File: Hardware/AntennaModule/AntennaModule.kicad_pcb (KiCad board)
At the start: 2 copper layers, 70 x 70 mm, 18 parts

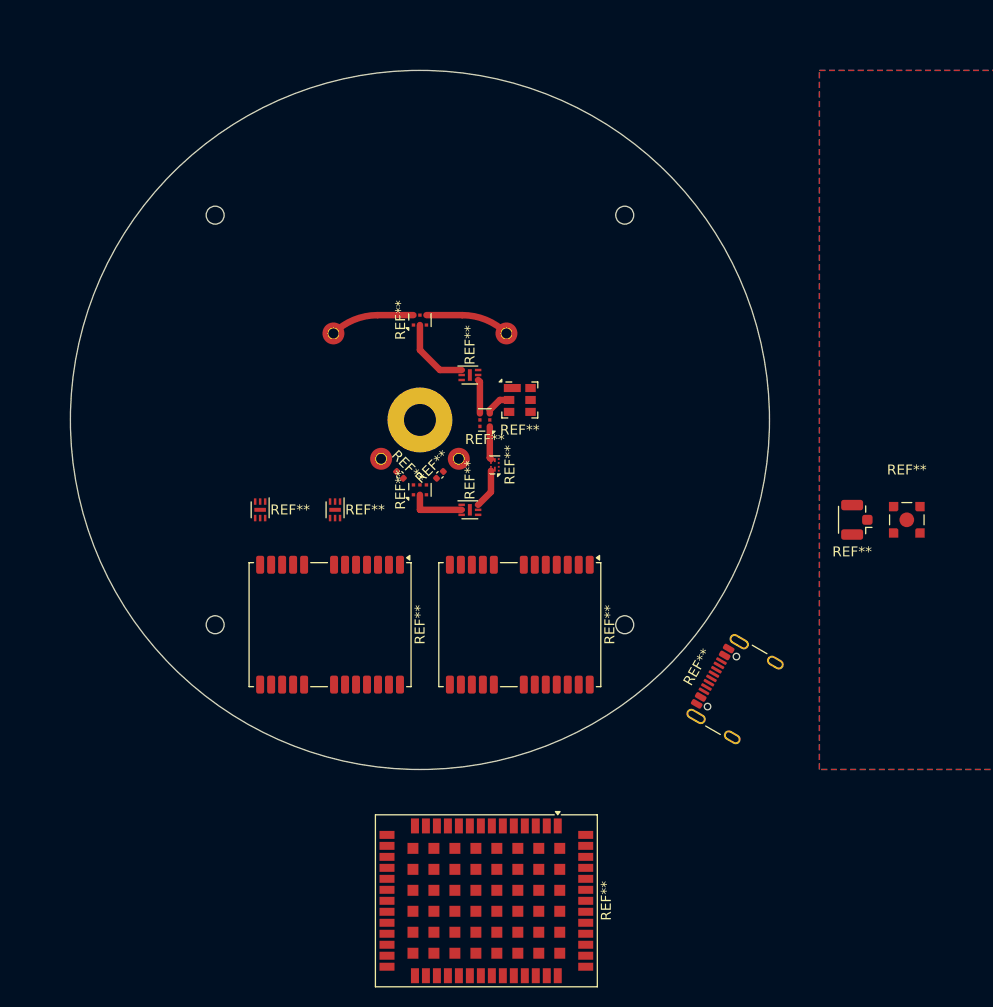
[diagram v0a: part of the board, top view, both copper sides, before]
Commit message: TE0149AをTE0133Bに変更
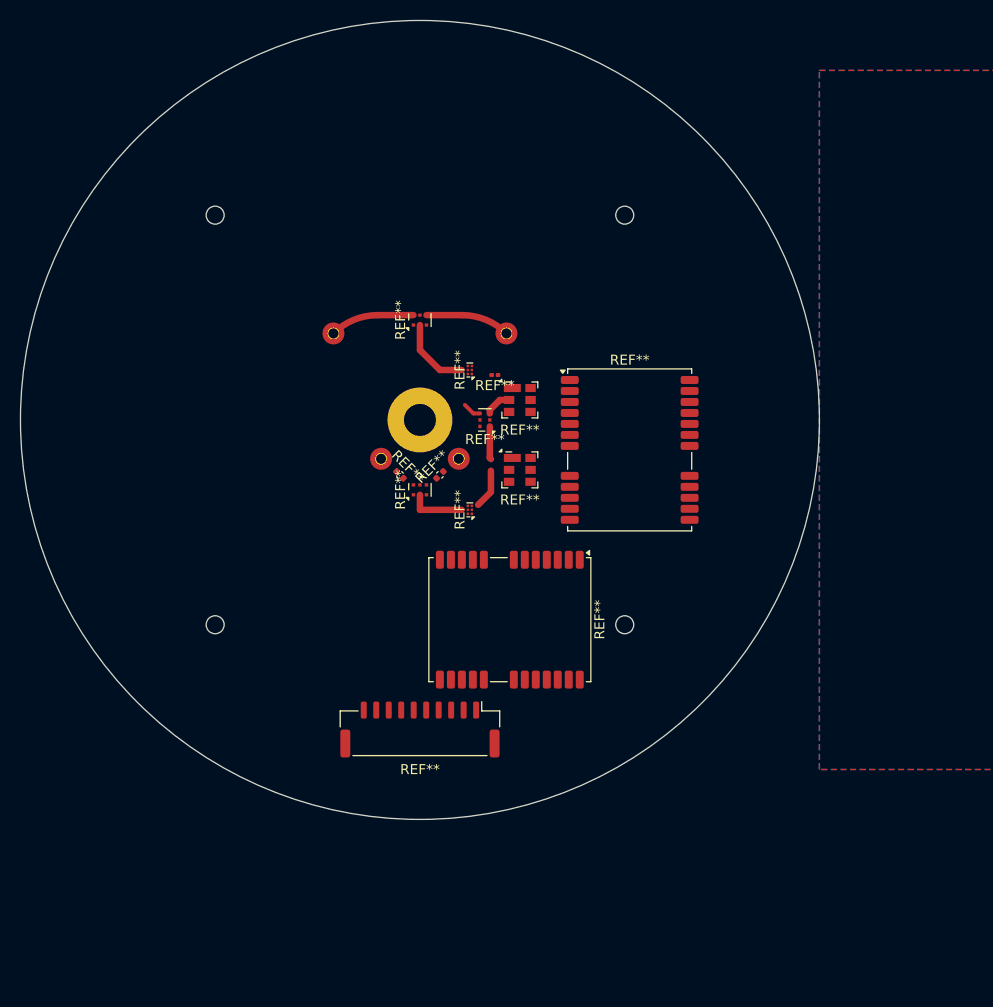
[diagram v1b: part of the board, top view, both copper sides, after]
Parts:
- removed the REF** at (150.0, 95.5)
- removed the REF** at (151.7, 148.2)
- removed the REF** at (193.8, 110.0)
- removed the REF** at (150.0, 109.0)
- removed the REF** at (152.5, 104.5)
- removed the REF** at (177.5, 127.5)
- removed the REF** at (188.8, 110.0)
- removed the REF** at (129.0, 109.0)
- removed the REF** at (136.5, 109.0)
- added REF**: JST_GH_BM10B-GHS-TBT_1x10-1MP_P1.25mm_Vertical, Connector_JST:JST_GH_BM10B-GHS-TBT_1x10-1MP_P1.25mm_Vertical, F.Cu at (145.0, 131.0)
- added REF**: Filter_SAW-6_3.0x3.0mm, Filter_extlib:Filter_SAW-6_3.0x3.0mm, F.Cu at (155.0, 105.0)
- added REF**: Nisshinbo_EPFFP-6-FA, RF_LNA_extlib:Nisshinbo_EPFFP-6-FA, F.Cu at (150.0, 95.0)
- added REF**: C_0201_0603Metric, Capacitor_SMD:C_0201_0603Metric, F.Cu at (152.5, 95.5)
- added REF**: Nisshinbo_EPFFP-6-FA, RF_LNA_extlib:Nisshinbo_EPFFP-6-FA, F.Cu at (150.0, 109.0)
- moved REF** 34.7 mm to (166.0, 103.0), turned to 0 degrees
- moved REF** 1.12 mm to (154.0, 120.0)
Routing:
- net (no net): track 43.5 -> 41.9 mm
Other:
- board size 70 x 70 mm -> 80 x 80 mm
- copper layers 2 -> 4

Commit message: 回路図完成
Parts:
- removed the REF** at (145.0, 131.0)
- removed the REF** at (151.5, 100.0)
- removed the REF** at (145.0, 107.0)
- removed the REF** at (166.0, 103.0)
- removed the REF** at (155.0, 105.0)
- removed the REF** at (145.0, 100.0)
- removed the REF** at (150.0, 95.0)
- removed the REF** at (152.5, 95.5)
- removed the REF** at (143.0, 105.5)
- removed the REF** at (150.0, 109.0)
- removed the REF** at (147.0, 105.5)
- removed the REF** at (155.0, 98.0)
- removed the REF** at (145.0, 90.0)
- removed the REF** at (154.0, 120.0)
- added REF**: L_Murata_LQW15ANxxxx80x_0402_1005Metric_1.0x0.6mm, Inductor_SMD_extlib:L_Murata_LQW15ANxxxx80x_0402_1005Metric_1.0x0.6mm, F.Cu at (150.6, 92.5)
- added REF**: Nisshinbo_EPFFP-6-FA, RF_LNA_extlib:Nisshinbo_EPFFP-6-FA, F.Cu at (152.0, 92.5)
- added REF**: Filter_SAW-6_3.0x3.0mm, Filter_extlib:Filter_SAW-6_3.0x3.0mm, F.Cu at (140.0, 100.0)
- added REF**: C_0402_1005Metric, Capacitor_SMD:C_0402_1005Metric, F.Cu at (153.2, 92.5)
- added REF**: Xinger_0805_2012Metric-6_Pad0.33x0.35mm, RF_Converter_extlib:Xinger_0805_2012Metric-6_Pad0.33x0.35mm, F.Cu at (143.0, 92.5)
- added REF**: Xinger_0805_2012Metric-6_Pad0.33x0.41mm, RF_Converter_extlib:Xinger_0805_2012Metric-6_Pad0.33x0.41mm, F.Cu at (156.5, 95.5)
- added REF**: R_Vishay_FC0603xxxxxxTxx_0603_1608Metric_1.626x0.813mm, Resistor_SMD_extlib:R_Vishay_FC0603xxxxxxTxx_0603_1608Metric_1.626x0.813mm, F.Cu at (158.0, 95.5)
- added REF**: L_Murata_LQW15ANxxxx80x_0402_1005Metric_1.0x0.6mm, Inductor_SMD_extlib:L_Murata_LQW15ANxxxx80x_0402_1005Metric_1.0x0.6mm, F.Cu at (145.0, 100.0)
- added REF**: C_0603_1608Metric, Capacitor_SMD:C_0603_1608Metric, F.Cu at (154.8, 92.5)
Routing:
- net (no net): track 41.9 -> 19.2 mm
- removed copper zone on B.Cu, net (none)
- removed copper zone on F.Cu, net (none)
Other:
- board outline removed
- copper layers 4 -> 2
- board text removed: "coupled"

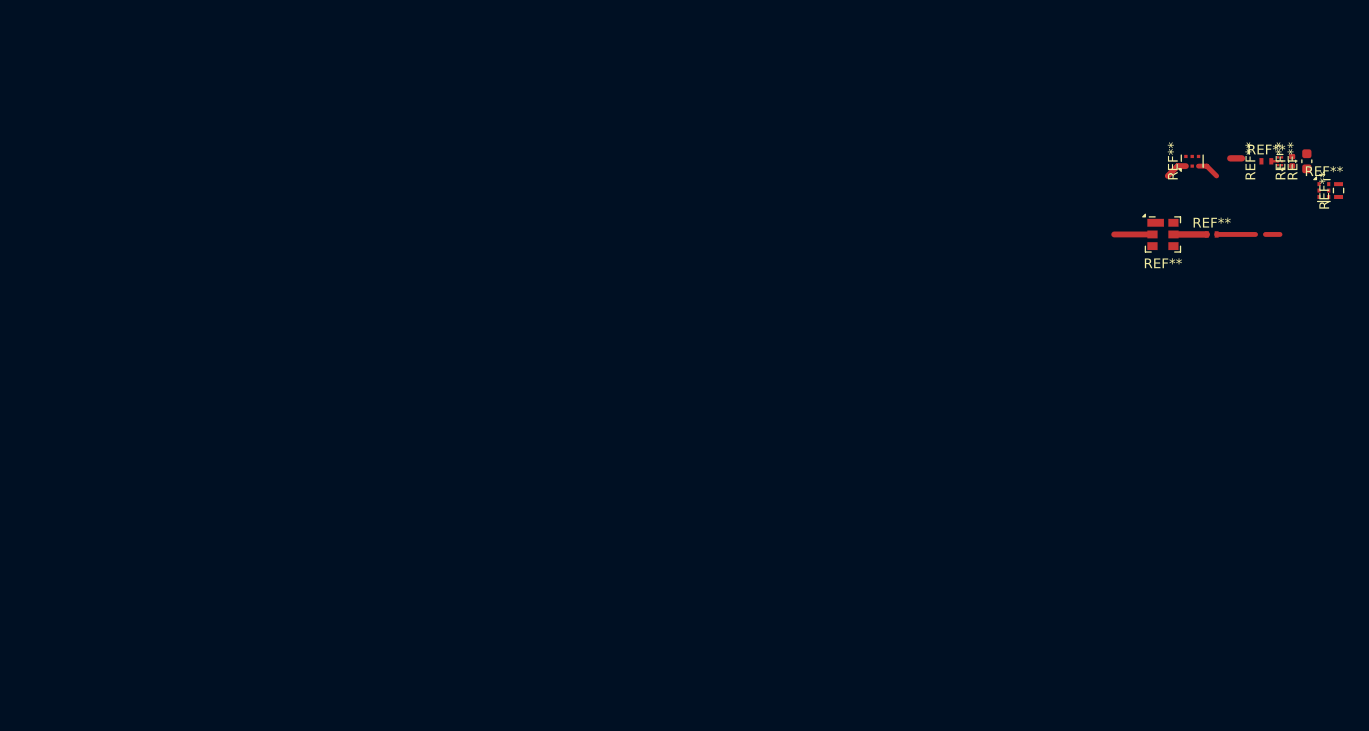
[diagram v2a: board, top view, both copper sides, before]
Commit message: アンテナの給電点が逆になっていたのを修正
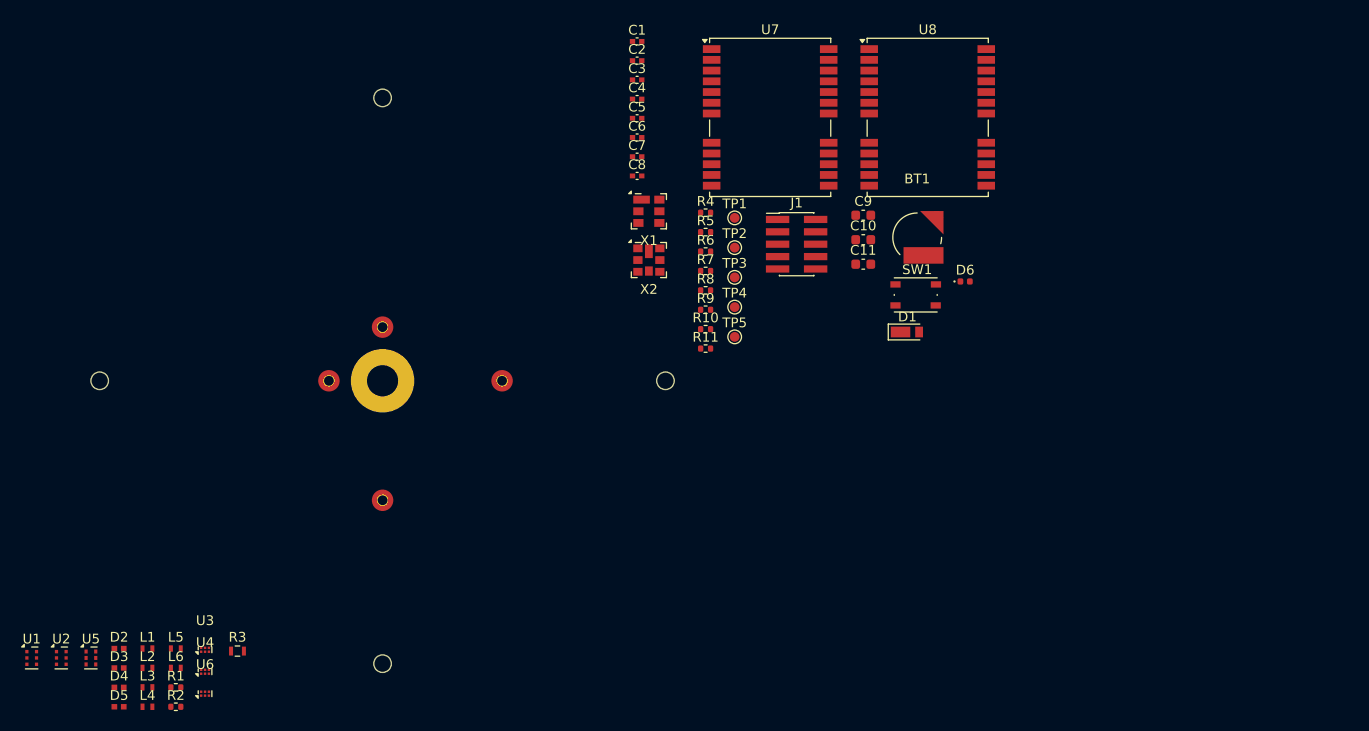
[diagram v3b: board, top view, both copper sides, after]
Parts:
- removed REF** (x2): L_Murata_LQW15ANxxxx80x_0402_1005Metric_1.0x0.6mm, Inductor_SMD_extlib:L_Murata_LQW15ANxxxx80x_0402_1005Metric_1.0x0.6mm
- removed REF**: Nisshinbo_EPFFP-6-FA, RF_LNA_extlib:Nisshinbo_EPFFP-6-FA
- removed REF**: Filter_SAW-6_3.0x3.0mm, Filter_extlib:Filter_SAW-6_3.0x3.0mm
- removed REF**: C_0402_1005Metric, Capacitor_SMD:C_0402_1005Metric
- removed REF**: Xinger_0805_2012Metric-6_Pad0.33x0.35mm, RF_Converter_extlib:Xinger_0805_2012Metric-6_Pad0.33x0.35mm
- removed REF**: Xinger_0805_2012Metric-6_Pad0.33x0.41mm, RF_Converter_extlib:Xinger_0805_2012Metric-6_Pad0.33x0.41mm
- removed REF**: R_Vishay_FC0603xxxxxxTxx_0603_1608Metric_1.626x0.813mm, Resistor_SMD_extlib:R_Vishay_FC0603xxxxxxTxx_0603_1608Metric_1.626x0.813mm
- removed REF**: C_0603_1608Metric, Capacitor_SMD:C_0603_1608Metric
- added AE1: GPDF6010.A, RF_Antenna_extlib:Taoglas_GPDF6010.A_GNSS, B.Cu at (60.0, 115.0)
- added BT1: MS421R, Battery_extlib:Battery_Seiko_MS421R, F.Cu at (114.8, 100.3)
- added C1: 4.7p, Capacitor_SMD_extlib:C_Murata_xxx15_0402_1005Metric_1.0x0.5mm, F.Cu at (86.1, 80.2)
- added C10: 2.2u, Capacitor_SMD:C_0603_1608Metric, F.Cu at (109.3, 100.5)
- added C11: 1u, Capacitor_SMD:C_0603_1608Metric, F.Cu at (109.3, 103.0)
- added C2: 4.7p, Capacitor_SMD_extlib:C_Murata_xxx15_0402_1005Metric_1.0x0.5mm, F.Cu at (86.1, 82.2)
- added C3: 1000p, Capacitor_SMD_extlib:C_Murata_xxx15_0402_1005Metric_1.0x0.5mm, F.Cu at (86.1, 84.2)
- added C4: 1000p, Capacitor_SMD_extlib:C_Murata_xxx15_0402_1005Metric_1.0x0.5mm, F.Cu at (86.1, 86.1)
- added C5: 2.4p, Capacitor_SMD_extlib:C_Murata_xxx15_0402_1005Metric_1.0x0.5mm, F.Cu at (86.1, 88.1)
- added C6: 1000p, Capacitor_SMD_extlib:C_Murata_xxx15_0402_1005Metric_1.0x0.5mm, F.Cu at (86.1, 90.1)
- added C7: 1p, Capacitor_SMD_extlib:C_Murata_xxx15_0402_1005Metric_1.0x0.5mm, F.Cu at (86.1, 92.0)
- added C8: 1p, Capacitor_SMD_extlib:C_Murata_xxx15_0402_1005Metric_1.0x0.5mm, F.Cu at (86.1, 94.0)
- added C9: 1u, Capacitor_SMD:C_0603_1608Metric, F.Cu at (109.3, 98.0)
- added D1: CUHS20S30, Diode_SMD_extlib:D_Toshiba_US2H, F.Cu at (113.8, 110.0)
- added D2: AXGD10402KR, Diode_SMD_extlib:D_Littelfuse_AXGD10402KR_0402_1005Metric_1.02x0.51mm, F.Cu at (33.0, 142.4)
- added D3: AXGD10402KR, Diode_SMD_extlib:D_Littelfuse_AXGD10402KR_0402_1005Metric_1.02x0.51mm, F.Cu at (33.0, 144.4)
- added D4: AXGD10402KR, Diode_SMD_extlib:D_Littelfuse_AXGD10402KR_0402_1005Metric_1.02x0.51mm, F.Cu at (33.0, 146.4)
- added D5: AXGD10402KR, Diode_SMD_extlib:D_Littelfuse_AXGD10402KR_0402_1005Metric_1.02x0.51mm, F.Cu at (33.0, 148.4)
- added D6: PULSE, LED_SMD:LED_0402_1005Metric, F.Cu at (119.7, 104.8)
- added J1: Conn_01x10, Connector_PinHeader_1.27mm:PinHeader_2x05_P1.27mm_Vertical_SMD, F.Cu at (102.4, 101.0)
- added L1: 12nH, Inductor_SMD_extlib:L_Murata_LQW15ANxxxx80x_0402_1005Metric_1.0x0.6mm, F.Cu at (35.9, 142.4)
- added L2: 20nH, Inductor_SMD_extlib:L_Murata_LQW15ANxxxx80x_0402_1005Metric_1.0x0.6mm, F.Cu at (35.9, 144.4)
- added L3: 3.3nH, Inductor_SMD_extlib:L_Murata_LQW15ANxxxx80x_0402_1005Metric_1.0x0.6mm, F.Cu at (35.9, 146.4)
- added L4: 5.6nH, Inductor_SMD_extlib:L_Murata_LQW15ANxxxx80x_0402_1005Metric_1.0x0.6mm, F.Cu at (35.9, 148.4)
- added L5: 3.6nH, Inductor_SMD_extlib:L_Murata_LQW15ANxxxx80x_0402_1005Metric_1.0x0.6mm, F.Cu at (38.8, 142.4)
- added L6: 20nH, Inductor_SMD_extlib:L_Murata_LQW15ANxxxx80x_0402_1005Metric_1.0x0.6mm, F.Cu at (38.8, 144.4)
- added R1: 50, Resistor_SMD:R_0402_1005Metric, F.Cu at (38.8, 146.4)
- added R10: 33, Resistor_SMD:R_0402_1005Metric, F.Cu at (93.1, 109.7)
- added R11: 1k, Resistor_SMD:R_0402_1005Metric, F.Cu at (93.1, 111.7)
- added R2: 50, Resistor_SMD:R_0402_1005Metric, F.Cu at (38.8, 148.4)
- added R3: 100, Resistor_SMD_extlib:R_Vishay_FC0603xxxxxxTxx_0603_1608Metric_1.626x0.813mm, F.Cu at (45.1, 142.7)
- added R4: 33, Resistor_SMD:R_0402_1005Metric, F.Cu at (93.1, 97.8)
- added R5: 33, Resistor_SMD:R_0402_1005Metric, F.Cu at (93.1, 99.8)
- added R6: 33, Resistor_SMD:R_0402_1005Metric, F.Cu at (93.1, 101.8)
- added R7: 33, Resistor_SMD:R_0402_1005Metric, F.Cu at (93.1, 103.7)
- added R8: 3.3k, Resistor_SMD:R_0402_1005Metric, F.Cu at (93.1, 105.7)
- added R9: 33, Resistor_SMD:R_0402_1005Metric, F.Cu at (93.1, 107.7)
- added SW1: ColdStart, Button_Switch_SMD:SW_Push_1P1T_NO_Vertical_Wuerth_434133025816, F.Cu at (114.7, 106.2)
- added TP1: ~{SAFEBOOT_F9P}, TestPoint:TestPoint_Pad_D1.0mm, F.Cu at (96.1, 98.3)
- added TP2: ~{SAFEBOOT_D9C}, TestPoint:TestPoint_Pad_D1.0mm, F.Cu at (96.1, 101.3)
- added TP3: EXTINT_F9P, TestPoint:TestPoint_Pad_D1.0mm, F.Cu at (96.1, 104.4)
- added TP4: EXTINT_D9C, TestPoint:TestPoint_Pad_D1.0mm, F.Cu at (96.1, 107.5)
- added TP5: LNA_EN, TestPoint:TestPoint_Pad_D1.0mm, F.Cu at (96.1, 110.5)
- added U1: C0727J5003AHF-1, RF_Converter_extlib:Xinger_0805_2012Metric-6_Pad0.33x0.35mm, F.Cu at (24.0, 143.4)
- added U2: C0727J5003AHF-1, RF_Converter_extlib:Xinger_0805_2012Metric-6_Pad0.33x0.35mm, F.Cu at (27.1, 143.4)
- added U3: NJG1155UX2, RF_LNA_extlib:Nisshinbo_EPFFP-6-FA, F.Cu at (41.8, 142.6)
- added U4: NT1192FAAE1S, RF_LNA_extlib:Nisshinbo_EPFFP-6-FA, F.Cu at (41.8, 144.8)
- added U5: PD0922J5050S2HF, RF_Converter_extlib:Xinger_0805_2012Metric-6_Pad0.33x0.41mm, F.Cu at (30.1, 143.4)
- added U6: NT1192FAAE1S, RF_LNA_extlib:Nisshinbo_EPFFP-6-FA, F.Cu at (41.8, 147.1)
- added U7: NEO-D9C, RF_GNSS_extlib:ublox_NEO, F.Cu at (99.7, 88.0)
- added U8: NEO-F9P, RF_GNSS_extlib:ublox_NEO, F.Cu at (115.9, 88.0)
- added X1: TA1985A, Filter_extlib:Filter_SAW-6_3.0x3.0mm, F.Cu at (87.3, 97.6)
- added X2: TE0133B, Filter_extlib:Filter_SAW-8_3.0x3.0mm, F.Cu at (87.3, 102.6)
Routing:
- net (no net): track 19.2 -> 0.00 mm

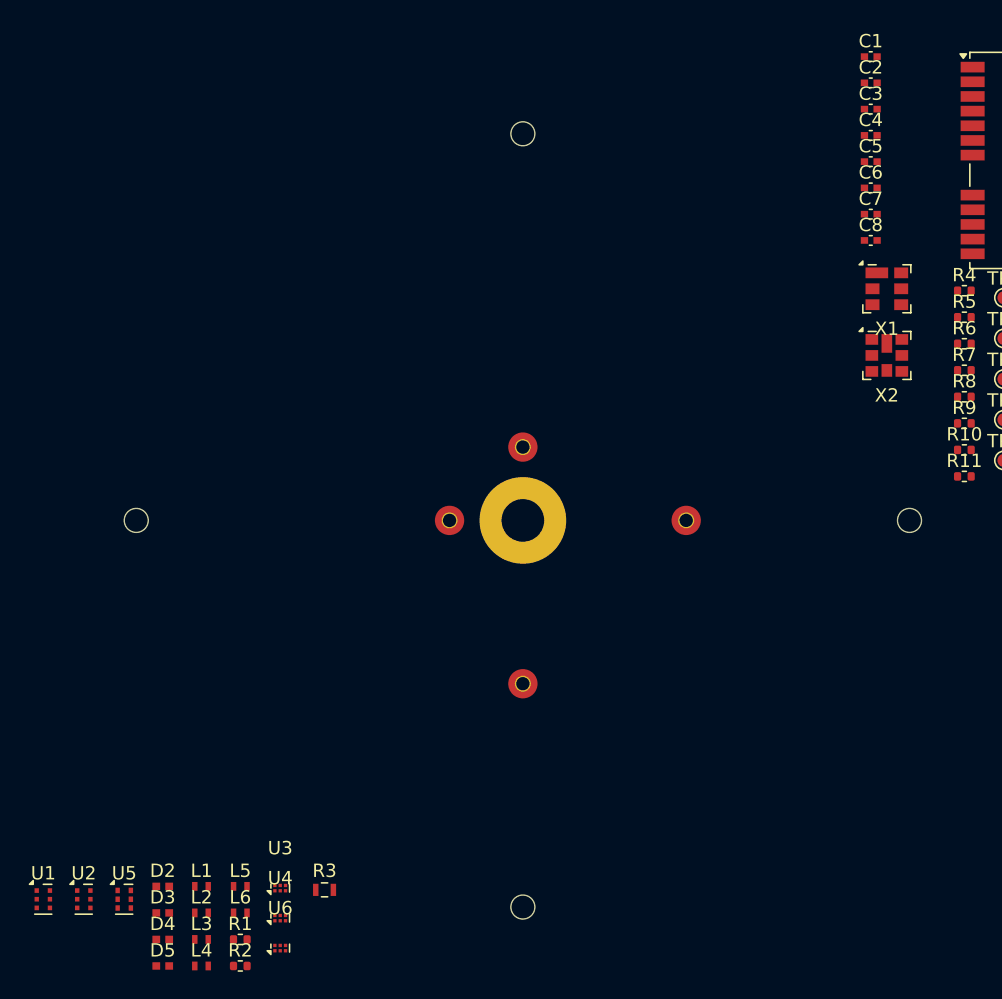
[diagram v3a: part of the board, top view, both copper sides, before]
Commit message: アンテナのFP修正に伴う回路図の修正
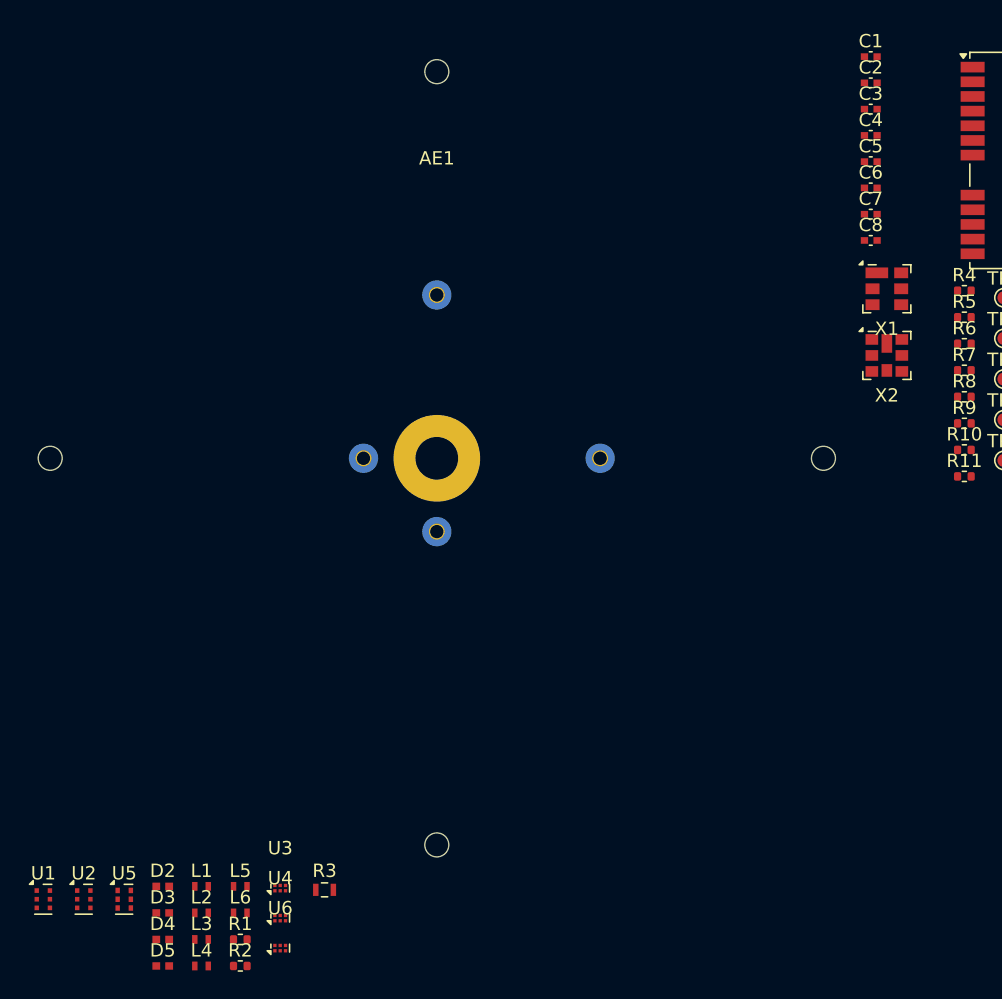
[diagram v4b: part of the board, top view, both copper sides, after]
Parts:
- AE1: moved to F.Cu
- moved AE1 7.96 mm to (53.5, 110.3)
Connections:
- AE1 pad 3: GND -> Net-(AE1B-LB1)
- AE1 pad 4: Net-(AE1B-LB1) -> Net-(AE1B-LB2)
- AE1 pad 5: Net-(AE1B-LB2) -> GND
